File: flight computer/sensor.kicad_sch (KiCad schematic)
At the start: 163 parts, among them IC1 A3909, J1 Micro_SD_Card_Det1, J12 Conn_01x04, J13 1x3 servo, J14 1x3 servo, J15 arming terminal, J16 arming terminal, J17 arming terminal, J18 arming terminal, J19 Screw_Terminal_01x02, J20 Screw_Terminal_01x02, J21 Screw_Terminal_01x02, J22 Screw_Terminal_01x02, J25 Conn_Coaxial, J3 Conn_Coaxial, J4 H9161TR-ND, J5 Screw_Term, J6 1x3 servo, J9 1x3 servo, Q1 IRLML6402, Q10 IRLML6402, Q11 IRLML6402, Q3 IRLML6402, Q4 IRLML6402, Q5 IRLML6402, Q6 IRLML6402, Q7 BSS138, Q8 IRLML6402, Q9 IRLML6402, U10 LSM6DS3, U11 BGM220SC12WGA2R, U12 PE4259, U2 IMU, U5 LPS22HB, U6 GPS, U7 SX1276, U8 NAND, Y2 32.768kHz, Y4 32MHz

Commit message: Huge amount of PCB changes
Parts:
- J25, J3: footprint SMA_CONNECTOR:LPRS_SMA_CONNECTOR -> SMA:LPRS_SMA_CONNECTOR
- J4: footprint KiCADv6:BGM220SC12WGA2R -> U.FL:HRS_U.FL-R-SMT_01_
- U11: footprint KiCADv6:BGM220SC12WGA2R -> BGM220SC12WGA2R:BGM220SC12WGA2R
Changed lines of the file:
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@@
 			)
 		)
-		(property "Footprint" "SMA_CONNECTOR:LPRS_SMA_CONNECTOR"
+		(property "Footprint" "SMA:LPRS_SMA_CONNECTOR"
 			(at -6.35 91.44 0)
 			(effects
@@
 			)
 		)
-		(property "Footprint" "SMA_CONNECTOR:LPRS_SMA_CONNECTOR"
+		(property "Footprint" "SMA:LPRS_SMA_CONNECTOR"
 			(at 113.03 45.72 0)
 			(effects
@@
 			)
 		)
-		(property "Footprint" "KiCADv6:BGM220SC12WGA2R"
+		(property "Footprint" "BGM220SC12WGA2R:BGM220SC12WGA2R"
 			(at -83.82 81.28 0)
 			(effects
@@
 			)
 		)
-		(property "Footprint" "KiCADv6:BGM220SC12WGA2R"
+		(property "Footprint" "U.FL:HRS_U.FL-R-SMT_01_"
 			(at -49.53 196.85 0)
 			(effects

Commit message: Wired up the IMU's to the MCU
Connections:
- net CS_IMU1 is gone; now on net CS_IMU TMCU: R35.2, U2.18 (~{H_CS})
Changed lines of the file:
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@@
-		)
-	)
-	(global_label "CS_IMU1"
-		(shape input)
-		(at 196.85 53.34 180)
-		(fields_autoplaced yes)
-		(effects
-			(font
-				(size 1.27 1.27)
-			)
-			(justify right)
-		)
-		(property "Intersheetrefs" "${INTERSHEET_REFS}"
-			(at 185.8215 53.34 0)
-			(effects
-				(font
-					(size 1.27 1.27)
-				)
-				(justify right)
-				(hide yes)
-			)
 		)
 	)
@@
 			(effects
 				(font
+					(size 1.27 1.27)
+				)
+				(justify right)
+				(hide yes)
+			)
+		)
+	)
+	(global_label "CS_IMU TMCU"
+		(shape input)
+		(at 196.85 53.34 180)
+		(fields_autoplaced yes)
+		(effects
+			(font
+				(size 1.27 1.27)
+			)
+			(justify right)
+		)
+		(property "Intersheetrefs" "${INTERSHEET_REFS}"
+			(at 181.0439 53.34 0)
+			(effects
+				(font

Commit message: Ummm, more baro routing to the MCU and stuff
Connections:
- net  SPI0_SCK MMCU is gone; now on net SPI0_SCK MMCU: U8.6 (CLK)
- net CS TMCU renamed SCK TMCU
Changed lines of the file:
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@@
 	(text "Baro"
 		(exclude_from_sim no)
-		(at 255.778 116.84 0)
+		(at 242.824 115.57 0)
 		(effects
 			(font
-				(size 1.27 1.27)
+				(size 2.032 2.032)
 			)
 		)
@@
 		)
 	)
-	(global_label " SPI0_SCK MMCU"
+	(global_label "SPI0_SCK MMCU"
 		(shape input)
 		(at 175.26 137.16 180)
@@
 		)
 		(property "Intersheetrefs" "${INTERSHEET_REFS}"
-			(at 155.8254 137.16 0)
+			(at 156.793 137.16 0)
 			(effects
 				(font
@@
 		)
 	)
-	(global_label "CS TMCU"
+	(global_label "SCK TMCU"
 		(shape input)
 		(at 251.46 100.33 0)
@@
 		)
 		(property "Intersheetrefs" "${INTERSHEET_REFS}"
-			(at 262.9118 100.33 0)
+			(at 264.1818 100.33 0)
 			(effects
 				(font

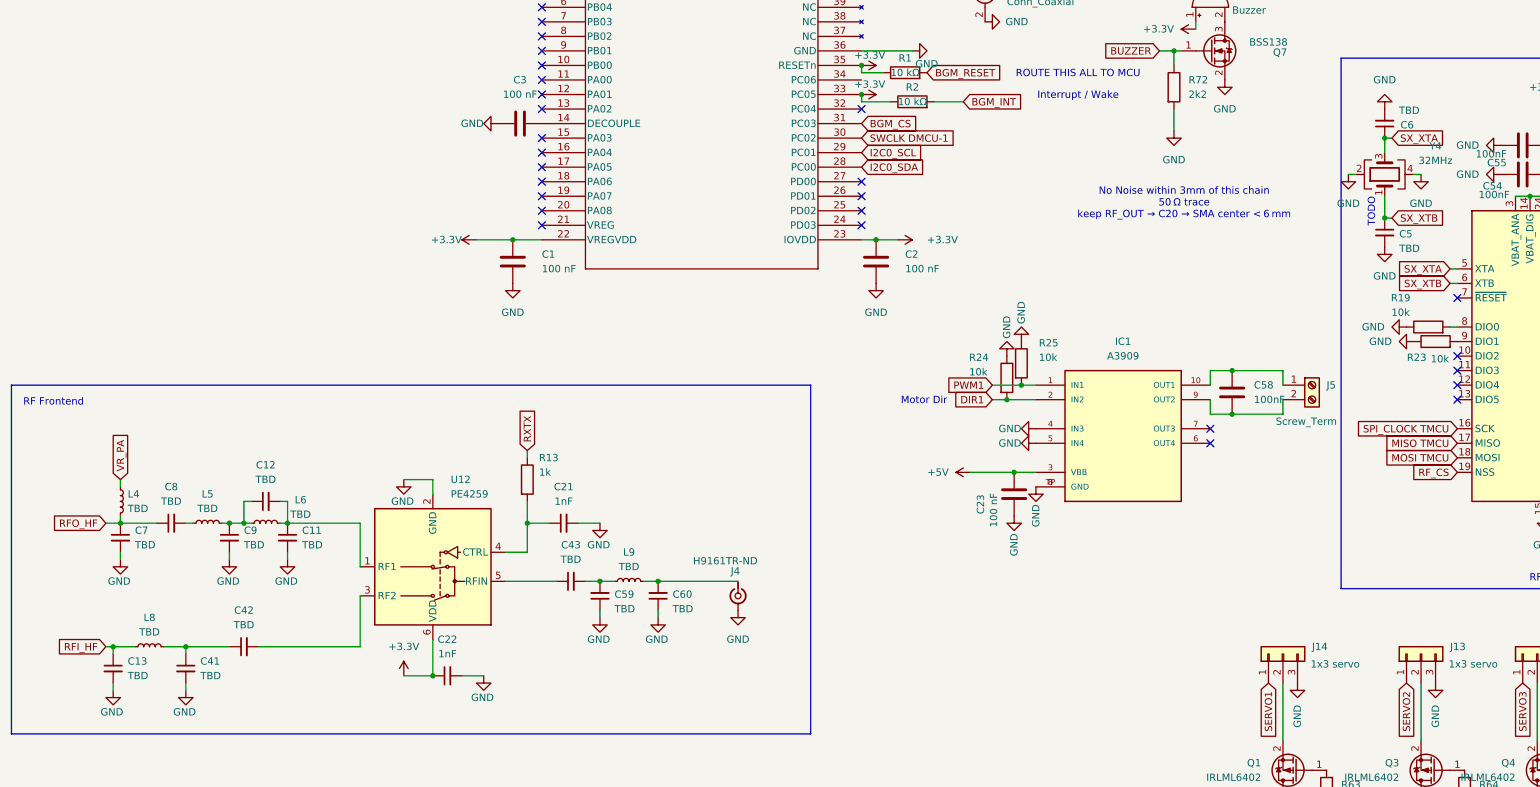
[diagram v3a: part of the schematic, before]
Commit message: Fixed the TBD's parts
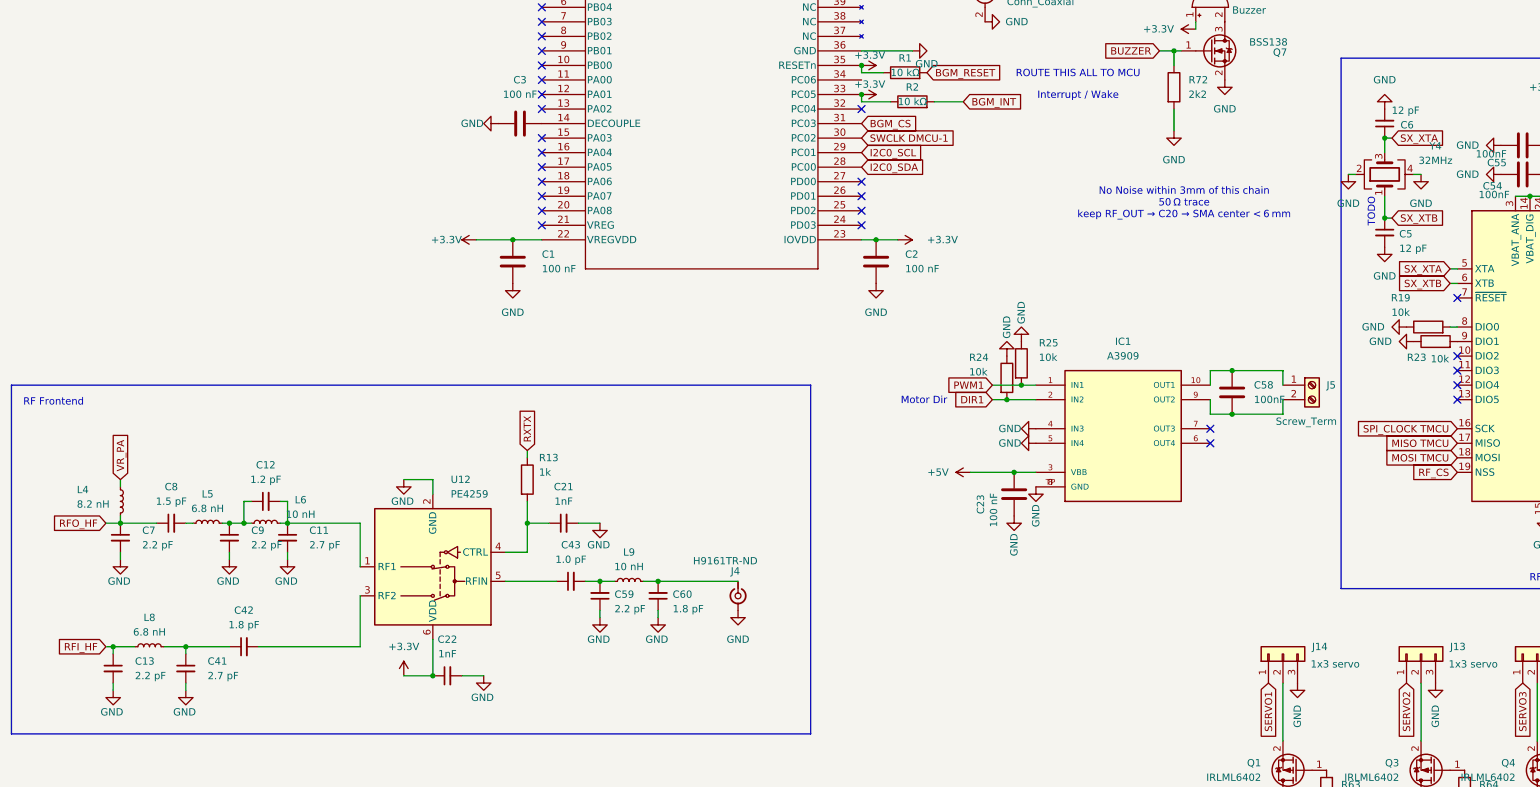
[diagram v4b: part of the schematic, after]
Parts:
- C11, C41: value TBD -> 2.7 pF
- C12: value TBD -> 1.2 pF
- C13, C59, C7, C9: value TBD -> 2.2 pF
- C42, C60: value TBD -> 1.8 pF
- C43: value TBD -> 1.0 pF
- C5, C6: value TBD -> 12 pF
- C8: value TBD -> 1.5 pF
- L4: value TBD -> 8.2 nH
- L5, L8: value TBD -> 6.8 nH
- L6, L9: value TBD -> 10 nH
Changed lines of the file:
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@@
 		(fields_autoplaced yes)
 		(property "Reference" "C41"
-			(at -143.51 208.2862 0)
+			(at -142.24 208.2862 0)
 			(effects
 				(font
@@
 			)
 		)
-		(property "Value" "TBD"
-			(at -143.51 210.8262 0)
+		(property "Value" "2.7 pF"
+			(at -142.24 210.8262 0)
 			(effects
 				(font
@@
 			)
 		)
-		(property "Value" "TBD"
+		(property "Value" "2.2 pF"
 			(at -71.12 199.136 0)
 			(effects
@@
 			)
 		)
-		(property "Value" "TBD"
+		(property "Value" "6.8 nH"
 			(at -152.4 203.2 90)
 			(effects
@@
 		(fields_autoplaced yes)
 		(property "Reference" "C13"
-			(at -156.21 208.2862 0)
+			(at -154.94 208.2862 0)
 			(effects
 				(font
@@
 			)
 		)
-		(property "Value" "TBD"
-			(at -156.21 210.8262 0)
+		(property "Value" "2.2 pF"
+			(at -154.94 210.8262 0)
 			(effects
 				(font
@@
 		(fields_autoplaced yes)
 		(property "Reference" "C7"
-			(at -154.94 185.4262 0)
+			(at -153.67 185.4262 0)
 			(effects
 				(font
@@
 			)
 		)
-		(property "Value" "TBD"
-			(at -154.94 187.9662 0)
+		(property "Value" "2.2 pF"
+			(at -153.67 187.9662 0)
 			(effects
 				(font
@@
 			)
 		)
-		(property "Value" "TBD"
+		(property "Value" "1.5 pF"
 			(at -148.5837 180.34 90)
 			(effects
@@
 			)
 		)
-		(property "Value" "TBD"
+		(property "Value" "10 nH"
 			(at -68.58 191.77 90)
 			(effects
@@
 			)
 		)
-		(property "Value" "TBD"
+		(property "Value" "1.8 pF"
 			(at -60.96 199.136 0)
 			(effects
@@
 		(on_board yes)
 		(dnp no)
-		(fields_autoplaced yes)
 		(property "Reference" "L4"
-			(at -156.21 179.0699 0)
+			(at -165.1 178.308 0)
 			(effects
 				(font
@@
 			)
 		)
-		(property "Value" "TBD"
-			(at -156.21 181.6099 0)
+		(property "Value" "8.2 nH"
+			(at -165.1 180.848 0)
 			(effects
 				(font
@@
 			)
 		)
-		(property "Value" "TBD"
+		(property "Value" "1.0 pF"
 			(at -78.7337 190.5 90)
 			(effects
@@
 		(fields_autoplaced yes)
 		(property "Reference" "C9"
-			(at -135.89 185.4262 0)
+			(at -134.62 185.4262 0)
 			(effects
 				(font
@@
 			)
 		)
-		(property "Value" "TBD"
-			(at -135.89 187.9662 0)
+		(property "Value" "2.2 pF"
+			(at -134.62 187.9662 0)
 			(effects
 				(font
@@
 			)
 		)
-		(property "Value" "TBD"
+		(property "Value" "6.8 nH"
 			(at -142.24 181.61 90)
 			(effects
@@
 			)
 		)
-		(property "Value" "TBD"
+		(property "Value" "1.8 pF"
 			(at -135.8837 201.93 90)
 			(effects
@@
 			)
 		)
-		(property "Value" "TBD"
+		(property "Value" "12 pF"
 			(at 66.04 136.144 0)
 			(effects
@@
 		(fields_autoplaced yes)
 		(property "Reference" "C11"
-			(at -125.73 185.4262 0)
+			(at -124.46 185.4262 0)
 			(effects
 				(font
@@
 			)
 		)
-		(property "Value" "TBD"
-			(at -125.73 187.9662 0)
+		(property "Value" "2.7 pF"
+			(at -124.46 187.9662 0)
 			(effects
 				(font
@@
 			)
 		)
-		(property "Value" "TBD"
+		(property "Value" "1.2 pF"
 			(at -132.0737 176.53 90)
 			(effects
@@
 			)
 		)
-		(property "Value" "TBD"
+		(property "Value" "12 pF"
 			(at 69.596 112.014 0)
 			(effects
@@
 			)
 		)
-		(property "Value" "TBD"
+		(property "Value" "10 nH"
 			(at -125.984 182.626 90)
 			(effects

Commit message: tspmo
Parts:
- removed C14: 0.1µF, Capacitor_SMD:C_0603_1608Metric, symbol Device:C
- removed C46, C47: 22pF, Capacitor_SMD:C_0603_1608Metric, symbol Device:C_Polarized_US
- removed C48, C49: 100nF, Capacitor_SMD:C_0603_1608Metric, symbol Device:C
- removed D5, D6: LED, LED_SMD:LED_0603_1608Metric, symbol Device:LED
- removed F3, F4: Polyfuse, Fuse:Fuse_0603_1608Metric, symbol Device:Polyfuse
- removed J17, J18: arming terminal, TerminalBlock_Phoenix:TerminalBlock_Phoenix_MPT-0,5-2-2.54_1x02_P2.54mm_Horizontal, symbol Connector:Screw_Terminal_01x02
- removed J21, J22: Screw_Terminal_01x02, TerminalBlock_Phoenix:TerminalBlock_Phoenix_MPT-0,5-2-2.54_1x02_P2.54mm_Horizontal, symbol Connector:Screw_Terminal_01x02
- removed Q10, Q11: IRLML6402, Package_TO_SOT_SMD:SOT-23, symbol Transistor_FET:IRLML6402
- removed R10, R8, R9: 10kΩ, Resistor_SMD:R_0603_1608Metric, symbol Device:R
- removed R31, R32, R33, R34, R35, R36, R82, R84: 10k, Resistor_SMD:R_0603_1608Metric, symbol Device:R
- removed R60, R61: 1k, Resistor_SMD:R_0603_1608Metric, symbol Device:R
- removed R83, R85: 100, Resistor_SMD:R_0603_1608Metric, symbol Device:R
- removed U2: IMU, BNO086:IC_BNO086, symbol BNO086:BNO086
- removed Y2: 32.768kHz, Crystal:Crystal_SMD_0603-2Pin_6.0x3.5mm, symbol Device:Crystal
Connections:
- no-connect marks 50 -> 47
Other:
- note removed: "IMU"
- moved on the sheet: C44, C45, R27, R37, R38, U10

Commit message: wiring + layout done
wiring and layout done
a lottt of stuff needs their 3v connected or 5v
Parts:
- J25, J3: footprint SMA:LPRS_SMA_CONNECTOR -> SMA_CONNECTOR:LPRS_SMA_CONNECTOR
- J4: footprint U.FL:HRS_U.FL-R-SMT_01_ -> U.FL-R-SMT_01_:HRS_U.FL-R-SMT_01_
- U11: footprint BGM220SC12WGA2R:BGM220SC12WGA2R -> KiCADv6:BGM220SC12WGA2R
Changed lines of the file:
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@@
 			)
 		)
-		(property "Footprint" "SMA:LPRS_SMA_CONNECTOR"
+		(property "Footprint" "SMA_CONNECTOR:LPRS_SMA_CONNECTOR"
 			(at -6.35 91.44 0)
 			(effects
@@
 			)
 		)
-		(property "Footprint" "SMA:LPRS_SMA_CONNECTOR"
+		(property "Footprint" "SMA_CONNECTOR:LPRS_SMA_CONNECTOR"
 			(at 113.03 45.72 0)
 			(effects
@@
 			)
 		)
-		(property "Footprint" "BGM220SC12WGA2R:BGM220SC12WGA2R"
+		(property "Footprint" "KiCADv6:BGM220SC12WGA2R"
 			(at -83.82 81.28 0)
 			(effects
@@
 			)
 		)
-		(property "Footprint" "U.FL:HRS_U.FL-R-SMT_01_"
+		(property "Footprint" "U.FL-R-SMT_01_:HRS_U.FL-R-SMT_01_"
 			(at -49.53 196.85 0)
 			(effects

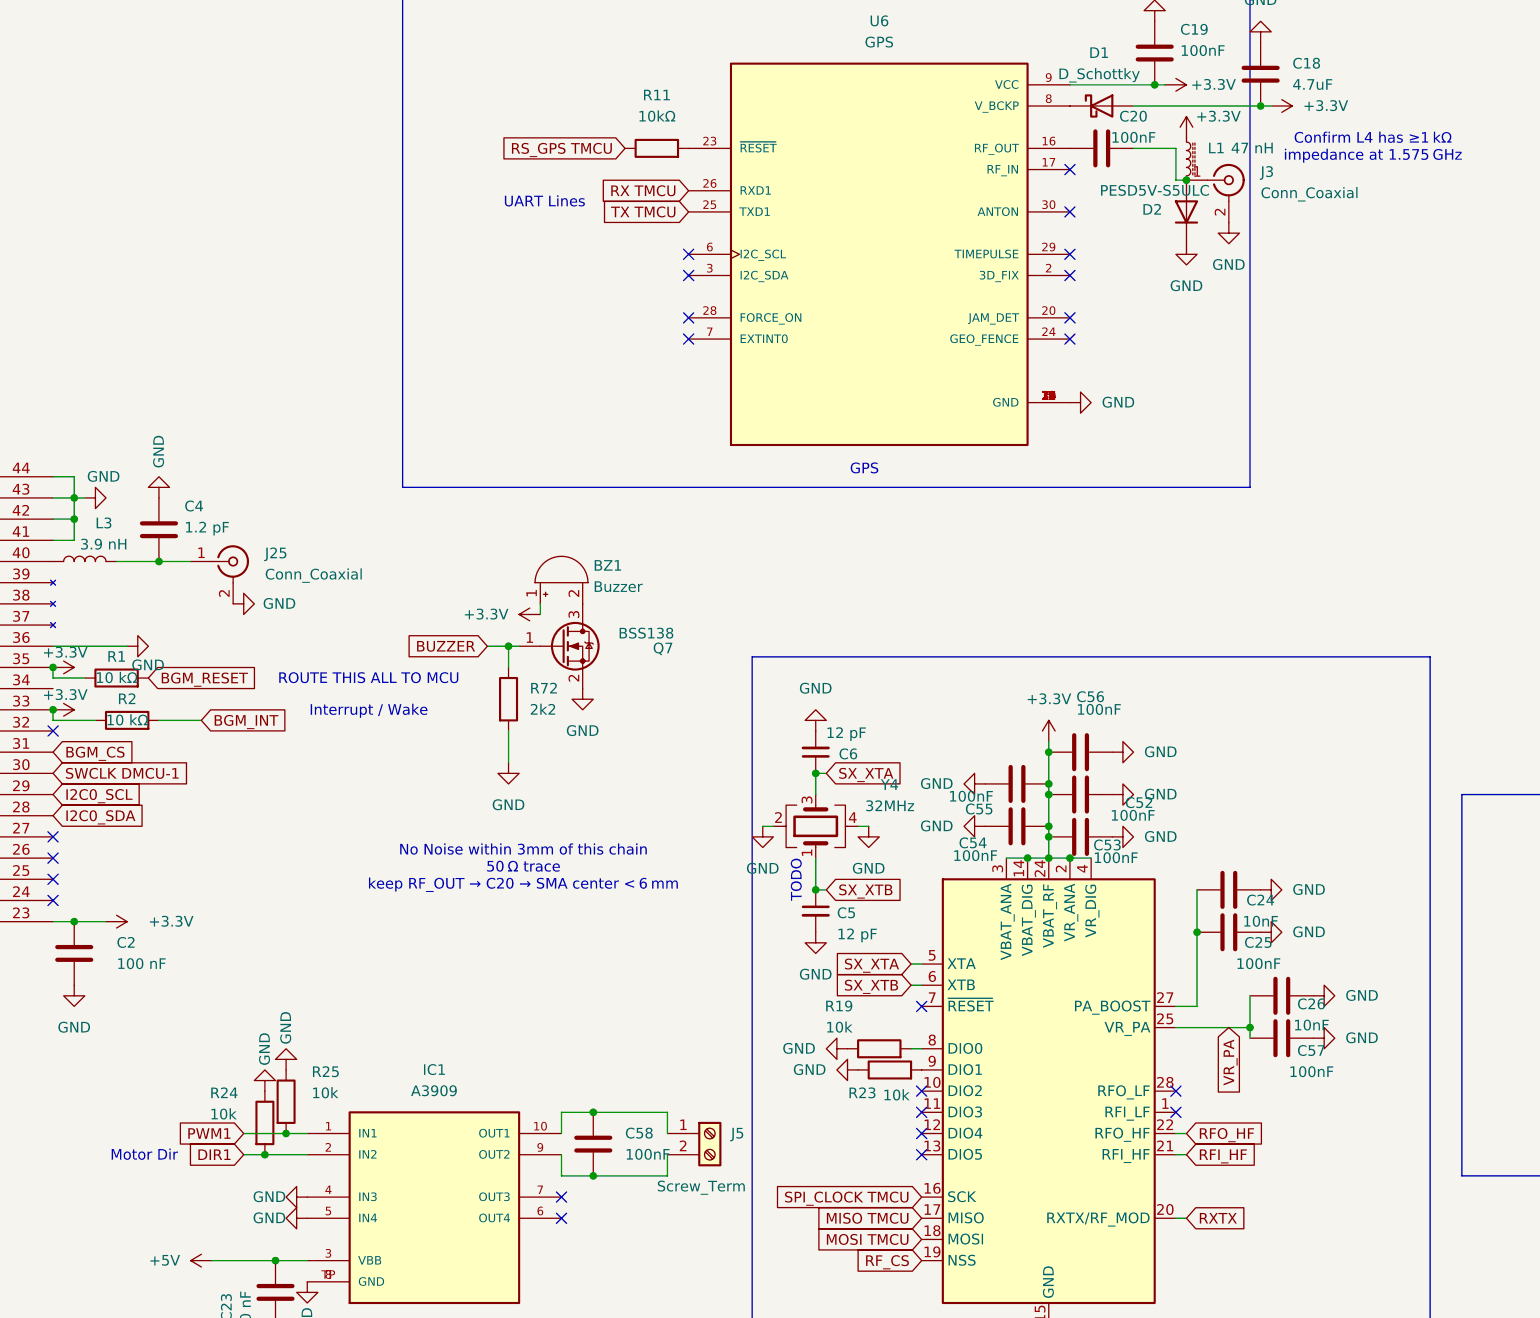
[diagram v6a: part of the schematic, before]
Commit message: Switched Bl and GPS to U.FL connectors
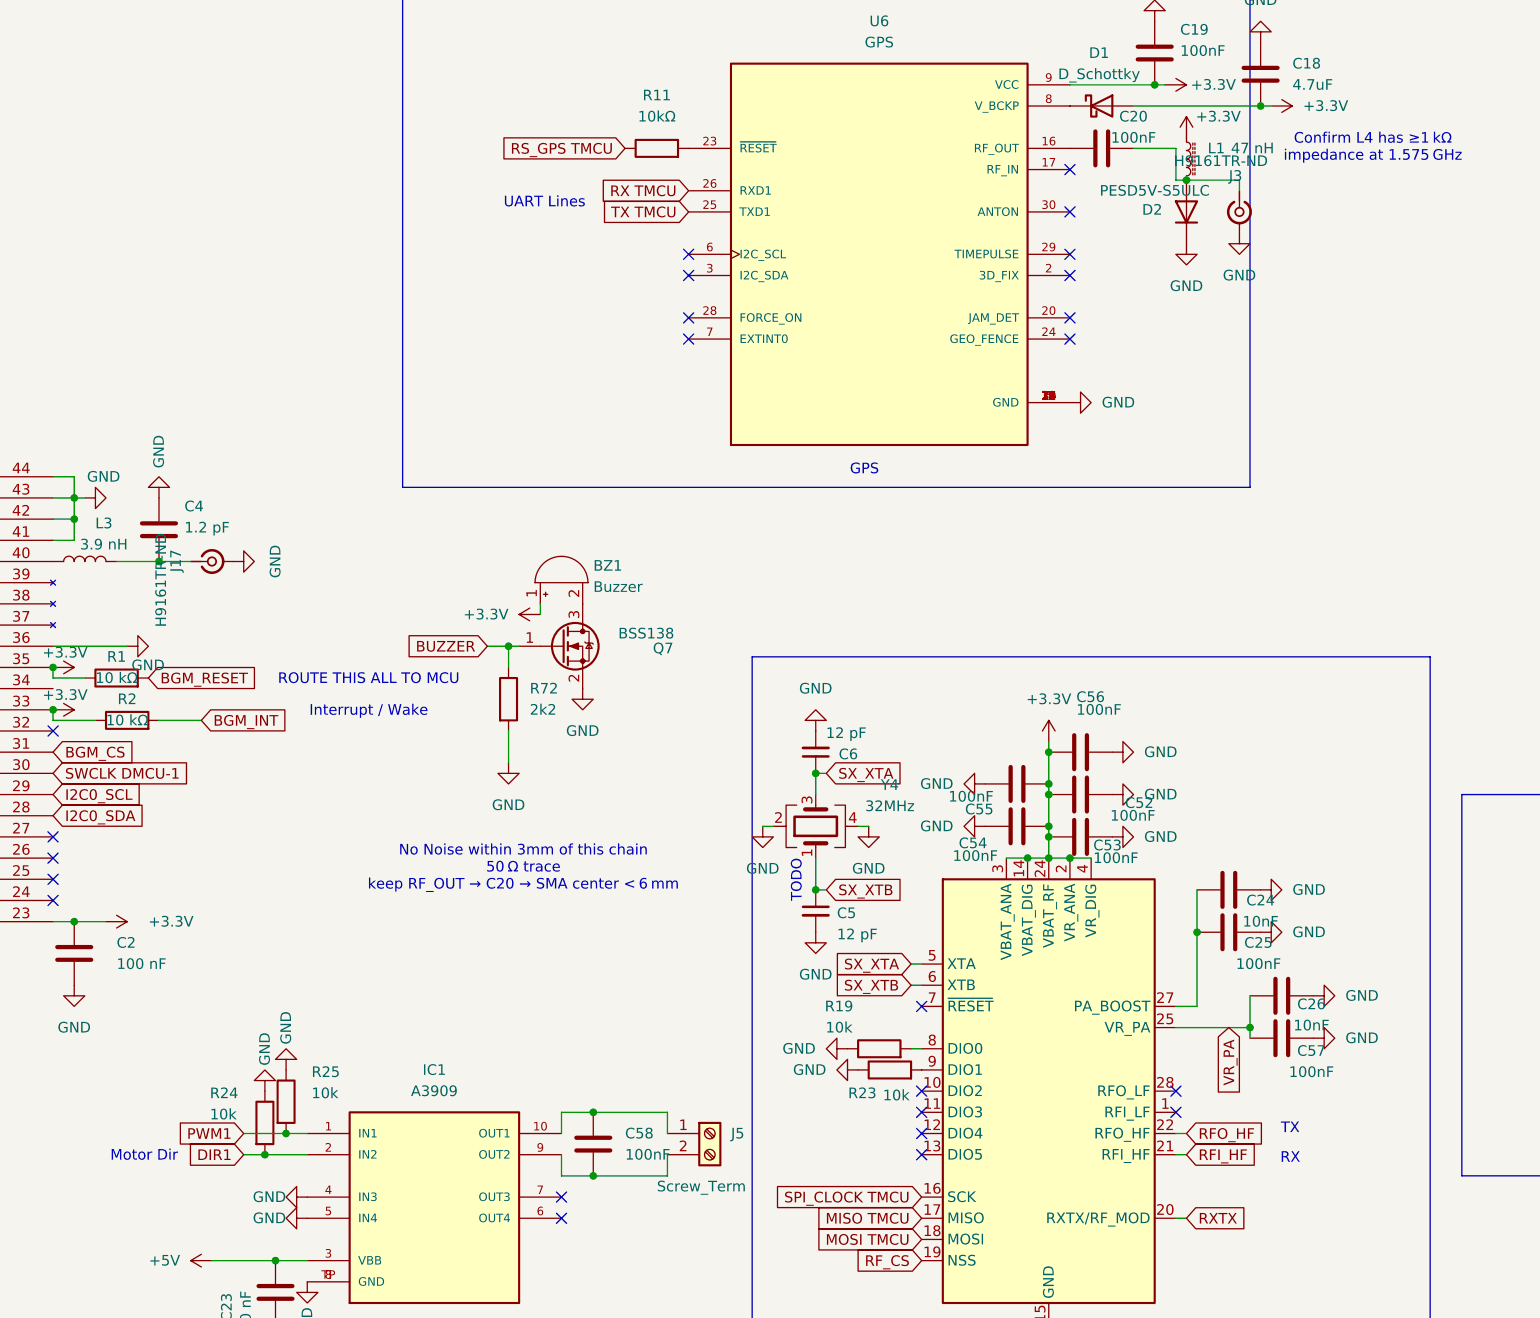
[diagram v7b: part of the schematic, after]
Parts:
- removed J25, J3: Conn_Coaxial, SMA_CONNECTOR:LPRS_SMA_CONNECTOR, symbol Connector:Conn_Coaxial
- added J17, J3: H9161TR-ND, U.FL-R-SMT_01_:HRS_U.FL-R-SMT_01_, symbol Connector:Conn_Coaxial_Small
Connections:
- net GND: now also J17.2 (Ext), J3.2 (Ext)
- net at C4.2, L3.2: now also J17.1 (In)
- net at C20.1, D2.2 (A), L1.2: now also J3.1 (In)
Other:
- note added: "RX"
- note added: "TX"
